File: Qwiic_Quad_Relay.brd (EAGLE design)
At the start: 82.5 x 47 mm, 110 parts, among them J2 Qwiic Right Angle, J3 Qwiic Right Angle, J4 AVR_SPI_PROG_3X2TESTPOINTS, J9 POWER_JACK, K1 RELAY-SPDT-JZC-11F, K2 RELAY-SPDT-JZC-11F, K3 RELAY-SPDT-JZC-11F, K4 RELAY-SPDT-JZC-11F, Q1 600mA/40V, Q2 600mA/40V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

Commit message: Ready for review
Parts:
- added U$50, U$51: (no value), Labels:QWIIC-LOGO-SMALL
- moved U$12 1.70 mm to (43.2, 45.7)
- moved U$14 1.70 mm to (43.2, 45.7)
- moved U$1 0.92 mm to (57.5, 46.2)
- moved C2 0.80 mm to (60.1, 41.3)
- moved C3 0.80 mm to (60.1, 39.8)
- moved C4 0.80 mm to (60.1, 37.0)
- moved D5 0.80 mm to (64.8, 27.9)
- moved D9 0.80 mm to (76.5, 30.5)
- moved J2 0.80 mm to (77.5, 37.0)
- moved J9 0.80 mm to (70.6, 51.3)
- moved Q1 0.80 mm to (68.6, 29.2)
- moved Q2 0.80 mm to (48.3, 29.2)
- moved R14 0.80 mm to (64.8, 29.6)
- moved R15 0.80 mm to (39.4, 27.9)
- moved R16 0.80 mm to (59.7, 27.9)
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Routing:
- net N$16: track 27.4 -> 29.5 mm
- net N$14: track 27.4 -> 29.3 mm
- net N$7: track 25.0 -> 27.0 mm
- net N$1: track 26.5 -> 28.4 mm
- net N$17: track 18.0 -> 19.3 mm
- net N$2: track 16.3 -> 17.5 mm
- net N$15: track 17.5 -> 18.8 mm
- net N$12: track 17.5 -> 18.8 mm
- net SDA/MOSI: track 111.1 -> 111.8 mm
- net 3.3V: track 82.2 -> 82.9 mm
- net 5V: track 138.3 -> 137.7 mm
- net OPTO_3: track 10.3 -> 9.71 mm
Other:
- board size 82.5 x 47 mm -> 82.5 x 48.3 mm
- board text added: "Units in Inches"

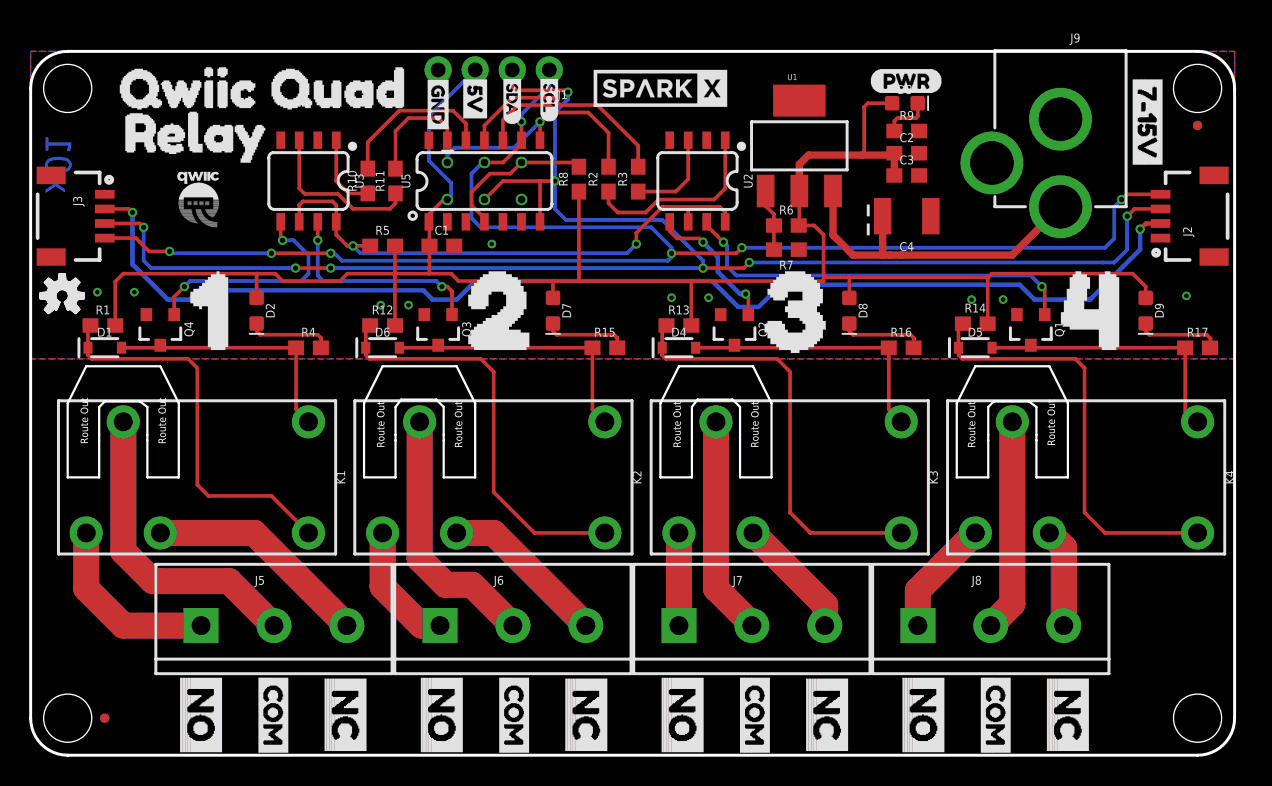
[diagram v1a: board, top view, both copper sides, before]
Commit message: Silk, diode, different  LEDs, jumper, rounded route out
I changed to better consistency of label size, a center positive label for the barrel jack, and added the new qwiic label to our new standard. Used different color LEDs so that a person could identify which relay is on by color. I added a jumper to bypass regulator in teh case they use a 5V Wall wart. Finally, I improved the route out - better shape, smaller size.
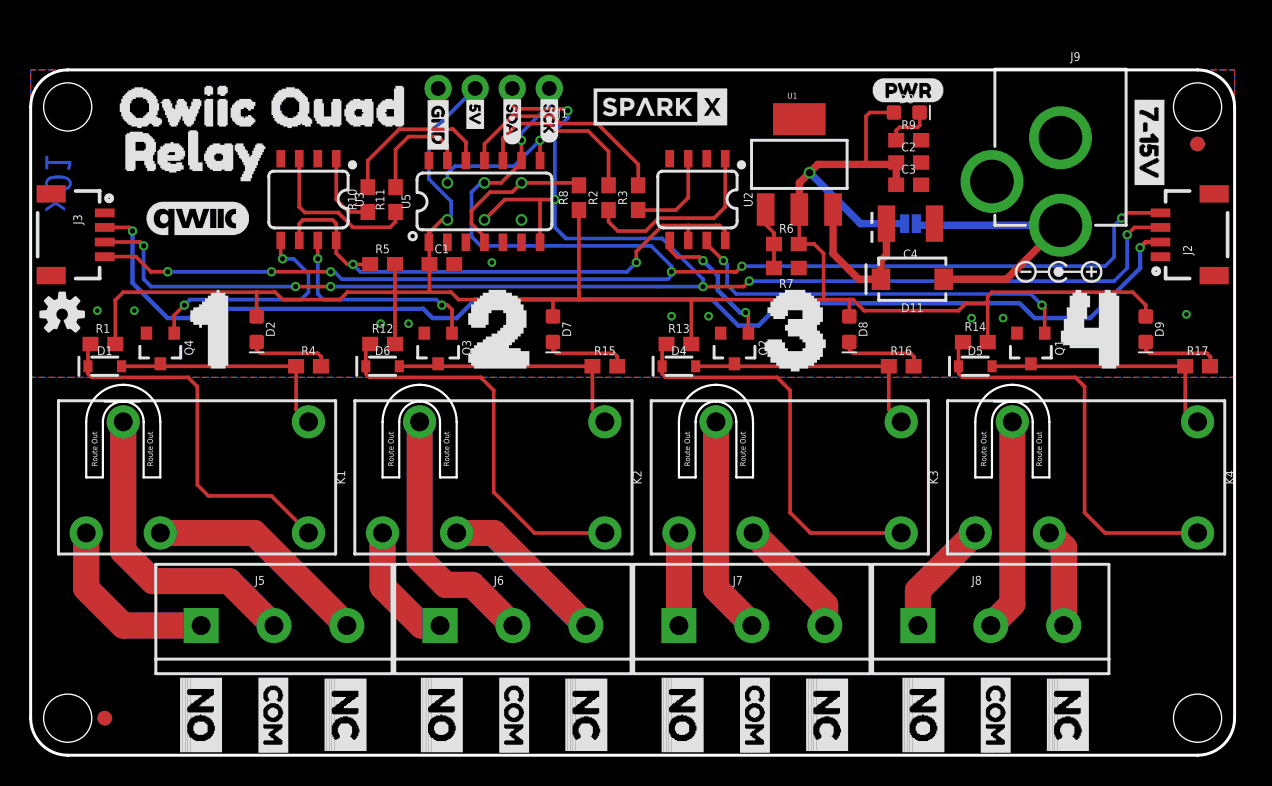
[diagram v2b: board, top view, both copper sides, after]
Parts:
- added D11: 1A/40V/500mV, SparkFun-DiscreteSemi:SMA-DIODE
- added JP7: JUMPER-SMT_2_NO_SILK, SparkFun-Jumpers:SMT-JUMPER_2_NO_SILK
- added U$52: (no value), jumper:JUMPER0
- added U$53: (no value), 7-15V:7#15V0
- added U$54: (no value), Polarity_marking_center_positive#jpg:POLARITY_MARKING_CENTER_POSITIVE#JPG
- added U$55, U$57: (no value), qwiic_copyrighted_logo_medium:QWIIC#JPG
- C4: value 47uF -> 10uF
- D2: value BLUE -> WHITE
- D8: value BLUE -> Yellow
- D9: value BLUE -> GREEN
- JP2, JP6, JP8, JP9: value FIDUCIALUFIDUCIAL -> FIDUCIAL1X2; device SparkFun:MICRO-FIDUCIAL -> SparkFun-Aesthetics:FIDUCIAL-1X2
- U$10: device SCL:SCL0 -> 5V:5V0
- U$46: device Labels:5V -> 5V:5V0
- U$48: device SCL:SCL0 -> Labels:SCK-[)-03
- U$50: device Labels:QWIIC-LOGO-SMALL -> 5V Wall Adapter:5V_WALL_ADAPTER0
- U$51: device Labels:QWIIC-LOGO-SMALL -> Polarity_marking_center_positive#jpg:POLARITY_MARKING_CENTER_POSITIVE#JPG
- U$8: device Labels:GND-03 -> Labels:SCK-[)-03
- U$9: device Labels:5V -> Labels:GND-03
- moved U$51 59.3 mm to (70.5, 33.1), flipped to the top
- moved U$50 55.5 mm to (66.8, 34.7), flipped to the bottom
- moved U$8 7.75 mm to (35.6, 45.3)
- moved U$10 5.27 mm to (30.5, 45.3)
- moved U$9 2.96 mm to (27.9, 45.3)
- moved U$46 1.52 mm to (30.5, 45.3)
- moved U$49 1.40 mm to (76.7, 45.6)
- moved J4 1.40 mm to (31.1, 38.0)
- moved U$11 1.40 mm to (33.0, 45.3)
- moved U$45 1.40 mm to (27.9, 45.3)
- moved U$47 1.40 mm to (33.0, 45.3)
- moved U$48 1.40 mm to (35.6, 45.3)
- moved U5 1.40 mm to (30.5, 38.0)
- moved J1 1.27 mm to (35.6, 45.7)
- moved J2 1.27 mm to (77.5, 35.7)
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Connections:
- new net VIN: D11.A, J9.PWR, JP7.1
- net 5V: now also JP7.2
- net N$4: now also D11.C; no longer J9.PWR
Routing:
- net VIN: track 0.00 -> 19.5 mm
- net N$4: track 23.2 -> 11.0 mm
- net 5V: track 137.7 -> 146.4 mm, vias 0 -> 1
- net N$14: track 29.3 -> 28.0 mm
- net N$16: track 29.5 -> 28.3 mm
- net N$17: track 19.3 -> 18.0 mm
- net N$7: track 27.0 -> 25.7 mm
- net N$2: track 17.5 -> 16.3 mm
- net N$15: track 18.8 -> 17.5 mm
- net N$12: track 18.8 -> 17.5 mm
- net N$1: track 28.4 -> 27.2 mm
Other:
- board size 82.5 x 48.3 mm -> 82.5 x 47 mm
- board text removed: "Units in Inches"
